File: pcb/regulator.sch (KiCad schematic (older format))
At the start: 24 parts, among them J1 Conn_01x06, U1 TL082

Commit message: Updated file structure, added logos to board, cleanup of schematics
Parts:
- added unit 3 of U1
- HG1: symbol Device:Hall_Generator -> regulator-rescue:Hall_Generator-Device
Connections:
- net labels added: GNDREF
- wire segments 76 -> 77
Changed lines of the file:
@@
 EESchema Schematic File Version 4
+LIBS:regulator-cache
 EELAYER 26 0
 EELAYER END
@@
 $EndDescr
 $Comp
-L Device:Hall_Generator HG1
+L regulator-rescue:Hall_Generator-Device HG1
 U 1 1 5C23856D
 P 2900 2400
@@
 U 2 1 5C2387B2
 P 3800 2500
-F 0 "U1" H 3800 2867 50  0000 C CNN
-F 1 "TL082" H 3800 2776 50  0000 C CNN
+F 0 "U1" H 3950 2400 50  0000 C CNN
+F 1 "TL082" H 3900 2300 50  0000 C CNN
 F 2 "Package_DIP:DIP-8_W7.62mm" H 3800 2500 50  0001 C CNN
 F 3 "http://www.ti.com/lit/ds/symlink/tl081.pdf" H 3800 2500 50  0001 C CNN
@@
 Connection ~ 2900 1550
 Wire Wire Line
-	2450 3300 6000 3300
+	2450 3300 5750 3300
 Wire Wire Line
 	6000 2850 6000 3300
@@
 	7500 1950 7500 1550
 Connection ~ 7500 1950
-$Comp
-L power:GND #PWR0101
-U 1 1 5C2533C5
-P 4550 2950
-F 0 "#PWR0101" H 4550 2700 50  0001 C CNN
-F 1 "GND" H 4555 2777 50  0000 C CNN
-F 2 "" H 4550 2950 50  0001 C CNN
-F 3 "" H 4550 2950 50  0001 C CNN
-	1    4550 2950
-	1    0    0    -1
-$EndComp
-$Comp
-L power:GND #PWR0102
-U 1 1 5C253407
-P 2350 2300
-F 0 "#PWR0102" H 2350 2050 50  0001 C CNN
-F 1 "GND" H 2200 2300 50  0000 C CNN
-F 2 "" H 2350 2300 50  0001 C CNN
-F 3 "" H 2350 2300 50  0001 C CNN
-	1    2350 2300
-	1    0    0    -1
-$EndComp
 Wire Wire Line
 	2350 2300 2450 2300
@@
 Wire Wire Line
 	6300 3300 6600 3300
-$Comp
-L power:GND #PWR0103
-U 1 1 5C2580F0
-P 2900 2700
-F 0 "#PWR0103" H 2900 2450 50  0001 C CNN
-F 1 "GND" H 2905 2527 50  0000 C CNN
-F 2 "" H 2900 2700 50  0001 C CNN
-F 3 "" H 2900 2700 50  0001 C CNN
-	1    2900 2700
-	1    0    0    -1
-$EndComp
 Wire Wire Line
 	2900 2600 2900 2700
-$Comp
-L power:GND #PWR0104
-U 1 1 5C25F2C6
-P 4050 2050
-F 0 "#PWR0104" H 4050 1800 50  0001 C CNN
-F 1 "GND" H 4055 1877 50  0000 C CNN
-F 2 "" H 4050 2050 50  0001 C CNN
-F 3 "" H 4050 2050 50  0001 C CNN
-	1    4050 2050
-	1    0    0    -1
-$EndComp
 Wire Wire Line
 	4050 2000 4050 2050
@@
 	7100 1550 7200 1550
 $Comp
-L power:VCC #PWR?
+L power:VCC #PWR0101
 U 1 1 5C2A455F
 P 2900 1550
-F 0 "#PWR?" H 2900 1400 50  0001 C CNN
+F 0 "#PWR0101" H 2900 1400 50  0001 C CNN
 F 1 "VCC" H 2917 1723 50  0000 C CNN
 F 2 "" H 2900 1550 50  0001 C CNN
@@
 	1    0    0    -1
 $EndComp
+$Comp
+L power:GNDREF #PWR0102
+U 1 1 5C58E8A1
+P 2350 2300
+F 0 "#PWR0102" H 2350 2050 50  0001 C CNN
+F 1 "GNDREF" H 2250 2350 50  0000 C CNN
+F 2 "" H 2350 2300 50  0001 C CNN
+F 3 "" H 2350 2300 50  0001 C CNN
+	1    2350 2300
+	1    0    0    -1
+$EndComp
+$Comp
+L power:GNDREF #PWR0103
+U 1 1 5C58EE44
+P 4050 2050
+F 0 "#PWR0103" H 4050 1800 50  0001 C CNN
+F 1 "GNDREF" H 4055 1877 50  0000 C CNN
+F 2 "" H 4050 2050 50  0001 C CNN
+F 3 "" H 4050 2050 50  0001 C CNN
+	1    4050 2050
+	1    0    0    -1
+$EndComp
+$Comp
+L power:GNDREF #PWR0104
+U 1 1 5C58EE81
+P 4550 2950
+F 0 "#PWR0104" H 4550 2700 50  0001 C CNN
+F 1 "GNDREF" H 4555 2777 50  0000 C CNN
+F 2 "" H 4550 2950 50  0001 C CNN
+F 3 "" H 4550 2950 50  0001 C CNN
+	1    4550 2950
+	1    0    0    -1
+$EndComp
+$Comp
+L power:GND #PWR0105
+U 1 1 5C58F035
+P 5750 3300
+F 0 "#PWR0105" H 5750 3050 50  0001 C CNN
+F 1 "GND" H 5755 3127 50  0000 C CNN
+F 2 "" H 5750 3300 50  0001 C CNN
+F 3 "" H 5750 3300 50  0001 C CNN
+	1    5750 3300
+	1    0    0    -1
+$EndComp
+$Comp
+L power:GNDREF #PWR0106
+U 1 1 5C59149F
+P 2900 2700
+F 0 "#PWR0106" H 2900 2450 50  0001 C CNN
+F 1 "GNDREF" H 3050 2700 50  0000 C CNN
+F 2 "" H 2900 2700 50  0001 C CNN
+F 3 "" H 2900 2700 50  0001 C CNN
+	1    2900 2700
+	1    0    0    -1
+$EndComp
+Connection ~ 5750 3300
+Wire Wire Line
+	5750 3300 6000 3300
+$Comp
+L Amplifier_Operational:TL082 U1
+U 3 1 5C5943D9
+P 3800 2500
+F 0 "U1" H 3750 2750 50  0001 L CNN
+F 1 "TL082" H 3750 2650 50  0001 L CNN
+F 2 "" H 3800 2500 50  0001 C CNN
+F 3 "http://www.ti.com/lit/ds/symlink/tl081.pdf" H 3800 2500 50  0001 C CNN
+	3    3800 2500
+	1    0    0    -1
+$EndComp
+$Comp
+L power:VCC #PWR?
+U 1 1 5C5953E2
+P 3700 2200
+F 0 "#PWR?" H 3700 2050 50  0001 C CNN
+F 1 "VCC" H 3717 2373 50  0000 C CNN
+F 2 "" H 3700 2200 50  0001 C CNN
+F 3 "" H 3700 2200 50  0001 C CNN
+	1    3700 2200
+	1    0    0    -1
+$EndComp
+$Comp
+L power:GND #PWR?
+U 1 1 5C5955BA
+P 3700 2800
+F 0 "#PWR?" H 3700 2550 50  0001 C CNN
+F 1 "GND" H 3600 2700 50  0000 C CNN
+F 2 "" H 3700 2800 50  0001 C CNN
+F 3 "" H 3700 2800 50  0001 C CNN
+	1    3700 2800
+	1    0    0    -1
+$EndComp

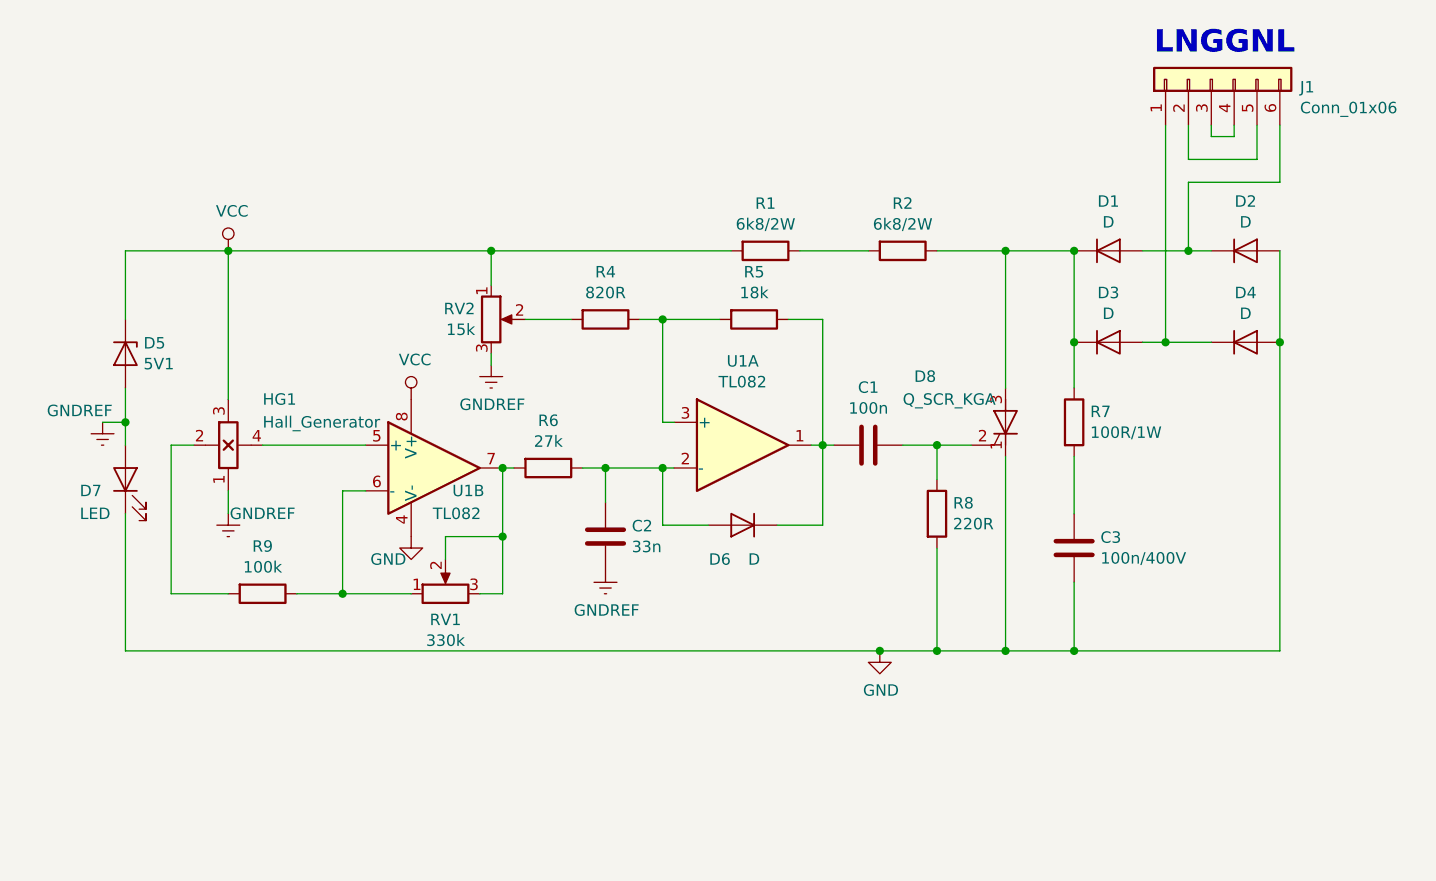
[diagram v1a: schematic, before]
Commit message: Update QR code, exchange of mounting hole (add vias to outline)
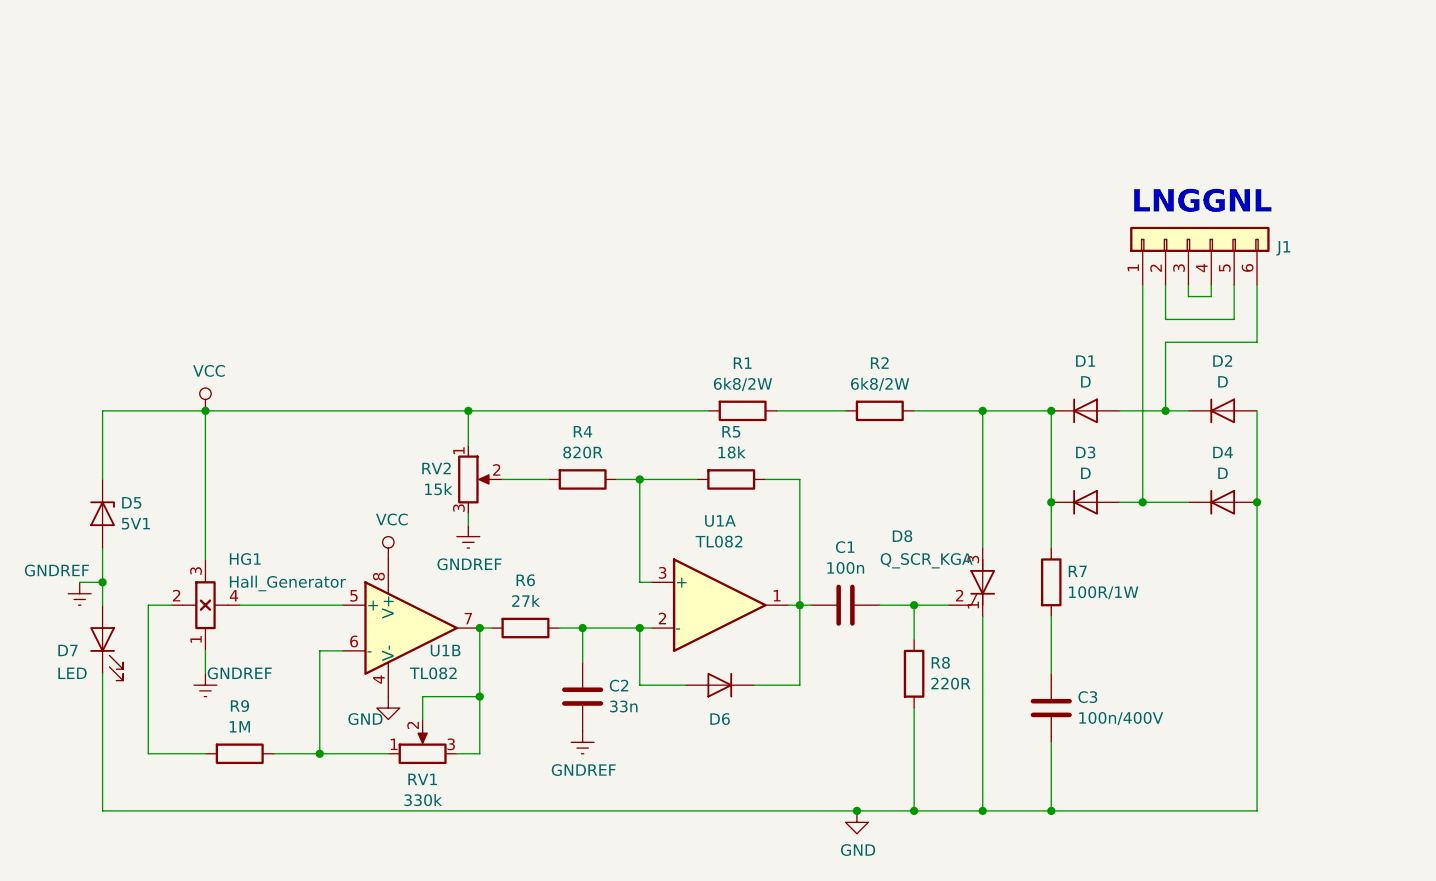
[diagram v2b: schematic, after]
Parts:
- R9: value 100k -> 1M
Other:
- moved on the sheet: C1, C2, C3, D1, D2, D3, D4, D5, D6, D7, D8, HG1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
